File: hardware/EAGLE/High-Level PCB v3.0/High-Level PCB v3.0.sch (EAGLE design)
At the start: 56 parts, among them IC1 MCP2551, IC2 DS8921, IC3 DS8921, J1 Optical Mouse, J3 Gyro, J4 Micro-SD, J7 ODO_JACK, J8 DB9 Plug, J9 CAN Output, U1 COMPASS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

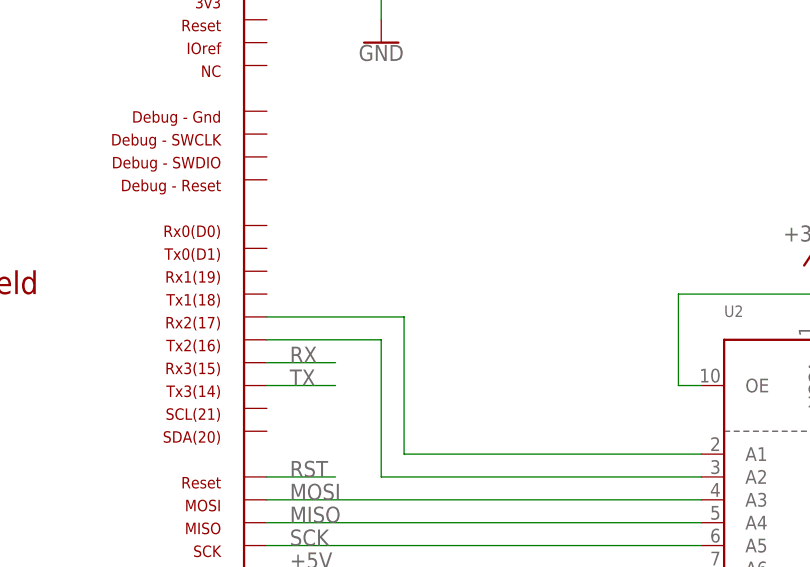
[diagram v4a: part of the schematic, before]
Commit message: Add files via upload
Added uart connection for raspberrypi
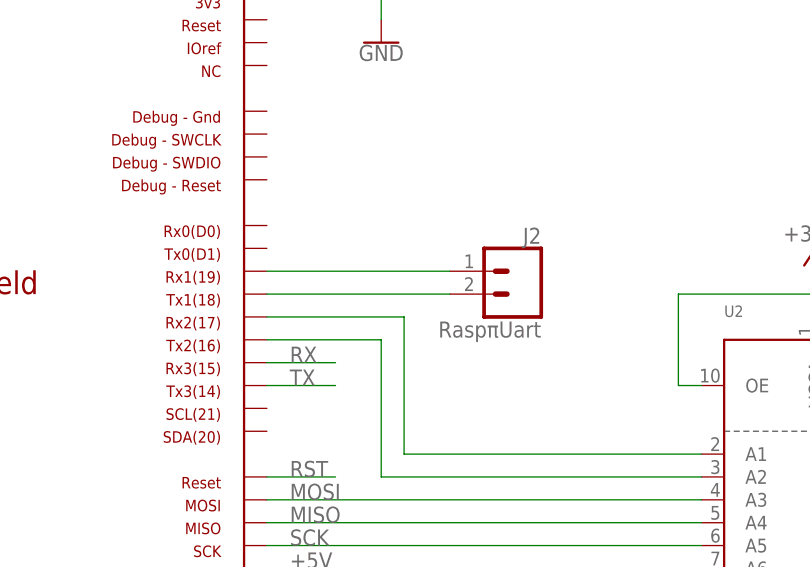
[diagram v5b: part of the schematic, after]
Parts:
- added J2: RaspπUart, tx_rxRasp:CONN_02
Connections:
- new net N$23: J2.2, MCU1.RX1
- new net N$24: J2.1, MCU1.TX1
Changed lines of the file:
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@@
 <grid distance="0.1" unitdist="inch" unit="inch" style="lines" multiple="1" display="no" altdistance="0.01" altunitdist="inch" altunit="inch"/>
 <layers>
-<layer number="1" name="Top" color="4" fill="1" visible="no" active="no"/>
-<layer number="2" name="Route2" color="1" fill="3" visible="no" active="no"/>
-<layer number="3" name="Route3" color="4" fill="3" visible="no" active="no"/>
-<layer number="4" name="Route4" color="1" fill="4" visible="no" active="no"/>
-<layer number="5" name="Route5" color="4" fill="4" visible="no" active="no"/>
-<layer number="6" name="Route6" color="1" fill="8" visible="no" active="no"/>
-<layer number="7" name="Route7" color="4" fill="8" visible="no" active="no"/>
-<layer number="8" name="Route8" color="1" fill="2" visible="no" active="no"/>
-<layer number="9" name="Route9" color="4" fill="2" visible="no" active="no"/>
-<layer number="10" name="Route10" color="1" fill="7" visible="no" active="no"/>
-<layer number="11" name="Route11" color="4" fill="7" visible="no" active="no"/>
-<layer number="12" name="Route12" color="1" fill="5" visible="no" active="no"/>
-<layer number="13" name="Route13" color="4" fill="5" visible="no" active="no"/>
-<layer number="14" name="Route14" color="1" fill="6" visible="no" active="no"/>
-<layer number="15" name="Route15" color="4" fill="6" visible="no" active="no"/>
-<layer number="16" name="Bottom" color="1" fill="1" visible="no" active="no"/>
-<layer number="17" name="Pads" color="2" fill="1" visible="no" active="no"/>
-<layer number="18" name="Vias" color="2" fill="1" visible="no" active="no"/>
-<layer number="19" name="Unrouted" color="6" fill="1" visible="no" active="no"/>
-<layer number="20" name="Dimension" color="15" fill="1" visible="no" active="no"/>
-<layer number="21" name="tPlace" color="7" fill="1" visible="no" active="no"/>
-<layer number="22" name="bPlace" color="7" fill="1" visible="no" active="no"/>
-<layer number="23" name="tOrigins" color="15" fill="1" visible="no" active="no"/>
-<layer number="24" name="bOrigins" color="15" fill="1" visible="no" active="no"/>
-<layer number="25" name="tNames" color="7" fill="1" visible="no" active="no"/>
-<layer number="26" name="bNames" color="7" fill="1" visible="no" active="no"/>
-<layer number="27" name="tValues" color="7" fill="1" visible="no" active="no"/>
-<layer number="28" name="bValues" color="7" fill="1" visible="no" active="no"/>
+<layer number="1" name="Top" color="4" fill="1" visible="yes" active="no"/>
+<layer number="2" name="Route2" color="1" fill="3" visible="yes" active="no"/>
+<layer number="3" name="Route3" color="4" fill="3" visible="yes" active="no"/>
+<layer number="4" name="Route4" color="1" fill="4" visible="yes" active="no"/>
+<layer number="5" name="Route5" color="4" fill="4" visible="yes" active="no"/>
+<layer number="6" name="Route6" color="1" fill="8" visible="yes" active="no"/>
+<layer number="7" name="Route7" color="4" fill="8" visible="yes" active="no"/>
+<layer number="8" name="Route8" color="1" fill="2" visible="yes" active="no"/>
+<layer number="9" name="Route9" color="4" fill="2" visible="yes" active="no"/>
+<layer number="10" name="Route10" color="1" fill="7" visible="yes" active="no"/>
+<layer number="11" name="Route11" color="4" fill="7" visible="yes" active="no"/>
+<layer number="12" name="Route12" color="1" fill="5" visible="yes" active="no"/>
+<layer number="13" name="Route13" color="4" fill="5" visible="yes" active="no"/>
+<layer number="14" name="Route14" color="1" fill="6" visible="yes" active="no"/>
+<layer number="15" name="Route15" color="4" fill="6" visible="yes" active="no"/>
+<layer number="16" name="Bottom" color="1" fill="1" visible="yes" active="no"/>
+<layer number="17" name="Pads" color="2" fill="1" visible="yes" active="no"/>
+<layer number="18" name="Vias" color="2" fill="1" visible="yes" active="no"/>
+<layer number="19" name="Unrouted" color="6" fill="1" visible="yes" active="no"/>
+<layer number="20" name="Dimension" color="15" fill="1" visible="yes" active="no"/>
+<layer number="21" name="tPlace" color="7" fill="1" visible="yes" active="no"/>
+<layer number="22" name="bPlace" color="7" fill="1" visible="yes" active="no"/>
+<layer number="23" name="tOrigins" color="15" fill="1" visible="yes" active="no"/>
+<layer number="24" name="bOrigins" color="15" fill="1" visible="yes" active="no"/>
+<layer number="25" name="tNames" color="7" fill="1" visible="yes" active="no"/>
+<layer number="26" name="bNames" color="7" fill="1" visible="yes" active="no"/>
+<layer number="27" name="tValues" color="7" fill="1" visible="yes" active="no"/>
+<layer number="28" name="bValues" color="7" fill="1" visible="yes" active="no"/>
 <layer number="29" name="tStop" color="7" fill="3" visible="no" active="no"/>
 <layer number="30" name="bStop" color="7" fill="6" visible="no" active="no"/>
@@
 <layer number="35" name="tGlue" color="7" fill="4" visible="no" active="no"/>
 <layer number="36" name="bGlue" color="7" fill="5" visible="no" active="no"/>
-<layer number="37" name="tTest" color="7" fill="1" visible="no" active="no"/>
-<layer number="38" name="bTest" color="7" fill="1" visible="no" active="no"/>
+<layer number="37" name="tTest" color="7" fill="1" visible="yes" active="no"/>
+<layer number="38" name="bTest" color="7" fill="1" visible="yes" active="no"/>
 <layer number="39" name="tKeepout" color="4" fill="11" visible="no" active="no"/>
 <layer number="40" name="bKeepout" color="1" fill="11" visible="no" active="no"/>
@@
 <layer number="44" name="Drills" color="7" fill="1" visible="no" active="no"/>
 <layer number="45" name="Holes" color="7" fill="1" visible="no" active="no"/>
-<layer number="46" name="Milling" color="3" fill="1" visible="no" active="no"/>
-<layer number="47" name="Measures" color="7" fill="1" visible="no" active="no"/>
-<layer number="48" name="Document" color="7" fill="1" visible="no" active="no"/>
-<layer number="49" name="Reference" color="7" fill="1" visible="no" active="no"/>
-<layer number="50" name="dxf" color="7" fill="1" visible="no" active="no"/>
-<layer number="51" name="tDocu" color="7" fill="1" visible="no" active="no"/>
-<layer number="52" name="bDocu" color="7" fill="1" visible="no" active="no"/>
-<layer number="53" name="tGND_GNDA" color="7" fill="9" visible="no" active="no"/>
-<layer number="54" name="bGND_GNDA" color="1" fill="9" visible="no" active="no"/>
-<layer number="56" name="wert" color="7" fill="1" visible="no" active="no"/>
-<layer number="57" name="tCAD" color="7" fill="1" visible="no" active="no"/>
-<layer number="59" name="tCarbon" color="7" fill="1" visible="no" active="no"/>
-<layer number="60" name="bCarbon" color="7" fill="1" visible="no" active="no"/>
+<layer number="46" name="Milling" color="3" fill="1" visible="yes" active="no"/>
+<layer number="47" name="Measures" color="7" fill="1" visible="yes" active="no"/>
+<layer number="48" name="Document" color="7" fill="1" visible="yes" active="no"/>
+<layer number="49" name="Reference" color="7" fill="1" visible="yes" active="no"/>
+<layer number="50" name="dxf" color="7" fill="1" visible="yes" active="no"/>
+<layer number="51" name="tDocu" color="7" fill="1" visible="yes" active="no"/>
+<layer number="52" name="bDocu" color="7" fill="1" visible="yes" active="no"/>
+<layer number="53" name="tGND_GNDA" color="7" fill="9" visible="yes" active="no"/>
+<layer number="54" name="bGND_GNDA" color="1" fill="9" visible="yes" active="no"/>
+<layer number="56" name="wert" color="7" fill="1" visible="yes" active="no"/>
+<layer number="57" name="tCAD" color="7" fill="1" visible="yes" active="no"/>
+<layer number="59" name="tCarbon" color="7" fill="1" visible="yes" active="no"/>
+<layer number="60" name="bCarbon" color="7" fill="1" visible="yes" active="no"/>
 <layer number="88" name="SimResults" color="9" fill="1" visible="yes" active="yes"/>
 <layer number="89" name="SimProbes" color="9" fill="1" visible="yes" active="yes"/>
@@
 <part name="U4" library="ELCOMPASS" deviceset="ELCOMPASS" device="" value="COMPASS"/>
 <part name="U3" library="ELGPS" deviceset="ELGPS" device="" value="GPS"/>
+<part name="J2" library="tx_rxRasp" deviceset="CONN_02" device="" value="RaspπUart"/>
 </parts>
 <sheets>
@@
 <instance part="U4" gate="G$1" x="60.96" y="127" rot="R90"/>
 <instance part="U3" gate="G$1" x="27.94" y="144.78" rot="MR0"/>
+<instance part="J2" gate="G$1" x="261.62" y="121.92" rot="MR0"/>
 </instances>
 <busses>
@@
 </segment>
 </net>
+<net name="N$23" class="0">
+<segment>
+<pinref part="J2" gate="G$1" pin="2"/>
+<pinref part="MCU1" gate="G$1" pin="RX1"/>
+<wire x1="254" y1="124.46" x2="233.68" y2="124.46" width="0.1524" layer="91"/>
+</segment>
+</net>
+<net name="N$24" class="0">
+<segment>
+<pinref part="J2" gate="G$1" pin="1"/>
+<pinref part="MCU1" gate="G$1" pin="TX1"/>
+<wire x1="254" y1="121.92" x2="233.68" y2="121.92" width="0.1524" layer="91"/>
+</segment>
+</net>
